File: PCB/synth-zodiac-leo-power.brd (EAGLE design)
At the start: 160 x 100 mm, 29 parts, among them J1 2.5 ID x 5.5 OD, J2 HDR-02P

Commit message: Snapshot of designs so far.
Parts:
- removed J1: 2.5 ID x 5.5 OD, con-jack:KLDX-0202
- added BOOST5: 5V Boost, regulators:POLOLU-U3V40FXX-SMD
- added BOOST9, BOOST9N: BOOST 9V, regulators:POLOLU-U3V40FXX-SMD
- added CONST: Leo, circuit-monkey-zodiac:LEO-CONST
- added GLYPH: Leo, circuit-monkey-zodiac:LEO-GLYPH
- added PCB: PCB FAB, circuit-monkey-zodiac:PENTAGON-40MM-RAD
- added PWR_AMP, PWR_COW, PWR_EG, PWR_KB, PWR_MIDI, PWR_VCA: (no value), con-jst:B4B-PH-SM4
- added VBAT: 2-pin, VT, SMT, con-jst:B2B-PH-SM4
- moved VREG9NEG 88.6 mm to (96.0, 10.0)
- renumbered J2 to 12V
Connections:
- new net VBAT: VBAT.1
- new net VIN: BOOST5.INA, BOOST5.INB, BOOST9.INA, BOOST9.INB, BOOST9N.INA, BOOST9N.INB
- new net VOUT: BOOST5.OUT, BOOST9.OUT, BOOST9N.OUT
- net +5V: now also PWR_AMP.3, PWR_COW.3, PWR_EG.3, PWR_KB.3, PWR_MIDI.3, PWR_VCA.3
- net +9V: now also PWR_AMP.1, PWR_COW.1, PWR_EG.1, PWR_KB.1, PWR_MIDI.1, PWR_VCA.1
- net -9V: now also PWR_AMP.2, PWR_COW.2, PWR_EG.2, PWR_KB.2, PWR_MIDI.2, PWR_VCA.2
- net GND: now also BOOST5.GNDA, BOOST5.GNDB, BOOST9.GNDA, BOOST9.GNDB, BOOST9N.GNDA, BOOST9N.GNDB, PCB.MTG1, PCB.MTG2, PCB.MTG3, PCB.MTG4, PCB.MTG5, PWR_AMP.4, PWR_COW.4, PWR_EG.4, PWR_KB.4, PWR_MIDI.4, PWR_VCA.4, VBAT.2; no longer J1.2A, J1.2B
- net N$1: no longer J1.1A, J1.1B
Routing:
- added copper zone on layer 1, net GND
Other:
- board size 160 x 100 mm -> 76.1 x 72.4 mm

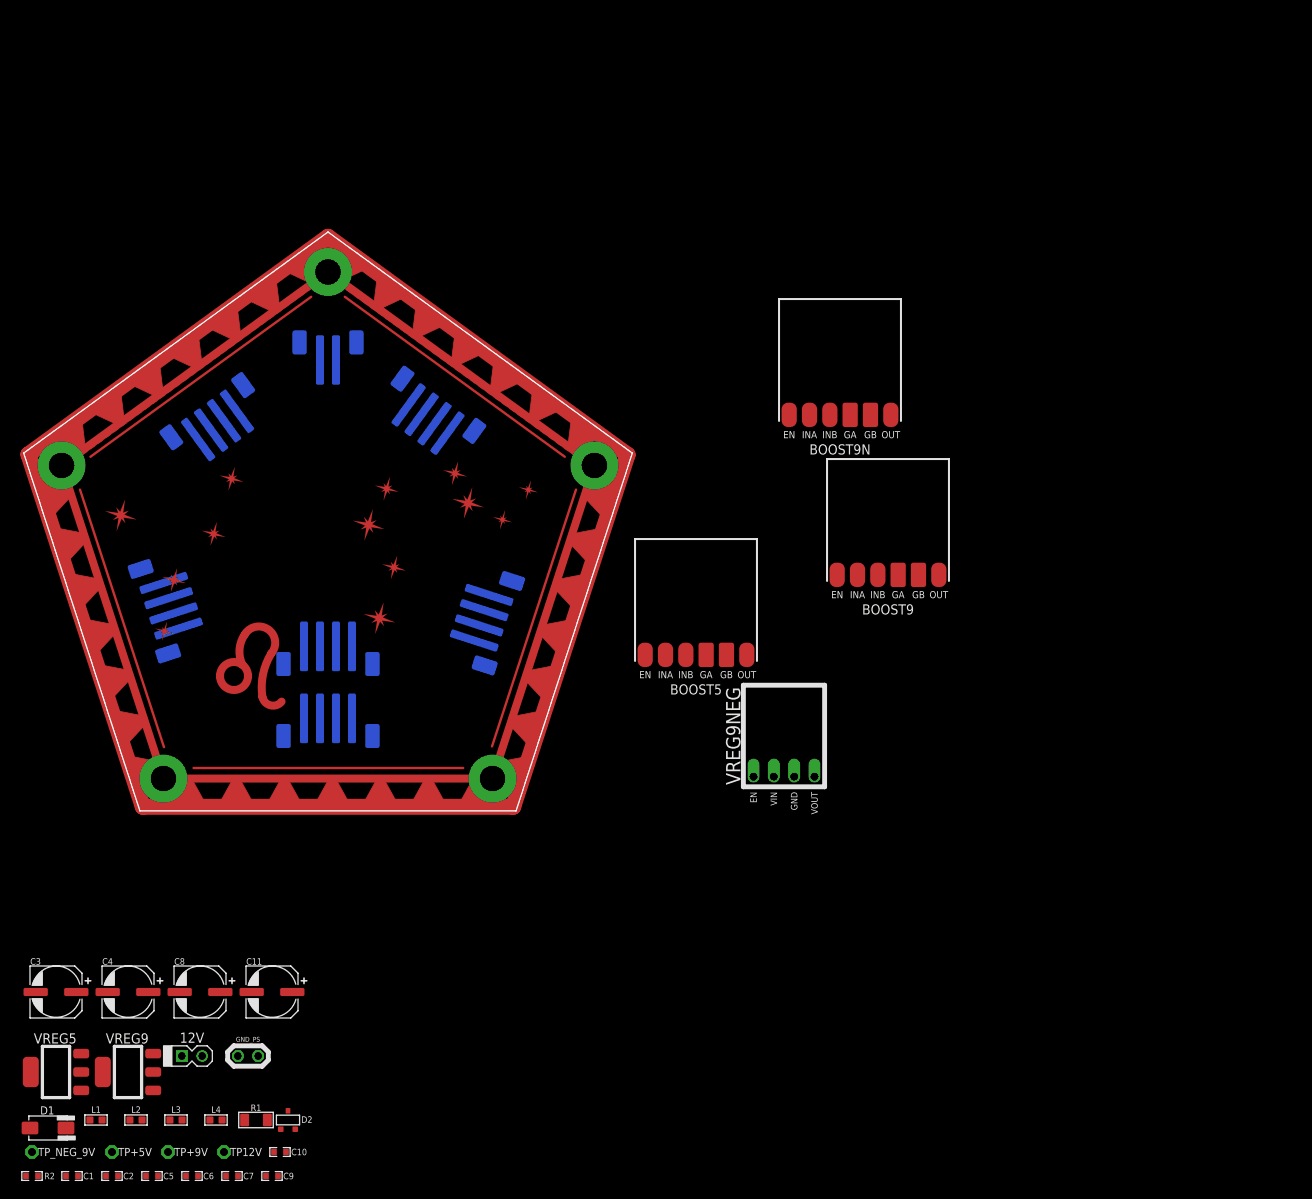
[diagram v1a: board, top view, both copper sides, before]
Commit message: Almost ready for FAB.
Sagittarius was mis-spelled, renamed it.  Taurus is still WIP.
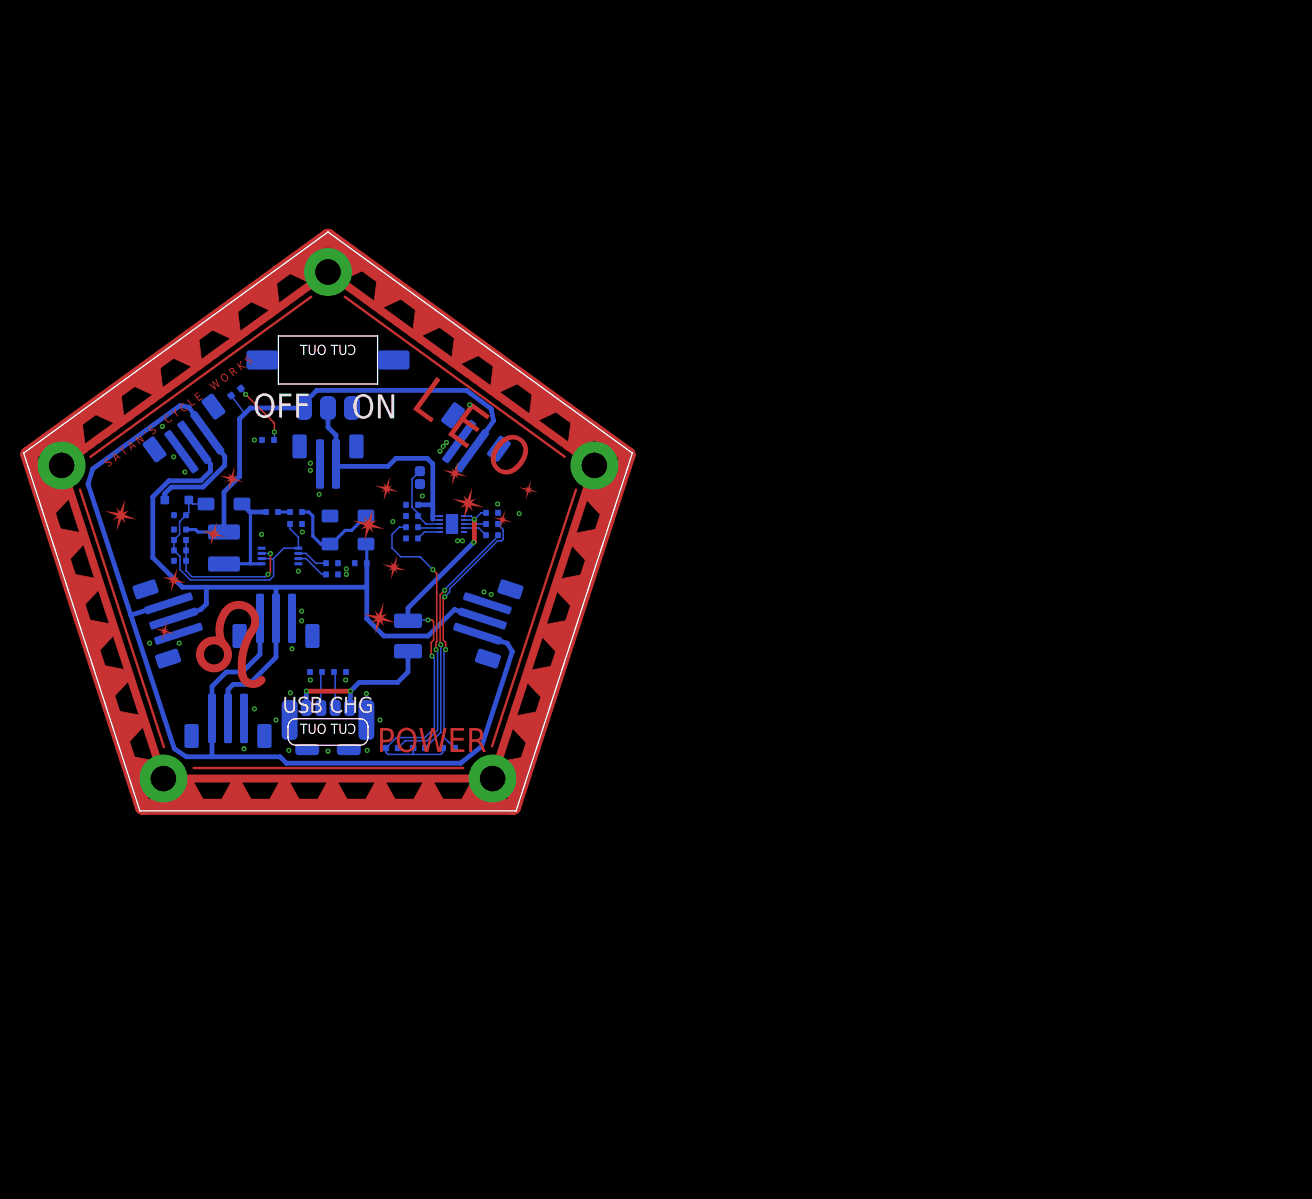
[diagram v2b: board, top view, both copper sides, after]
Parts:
- removed 12V: HDR-02P, con-headers:MA02X1-VT-THD
- removed BOOST5: 5V Boost, regulators:POLOLU-U3V40FXX-SMD
- removed BOOST9, BOOST9N: BOOST 9V, regulators:POLOLU-U3V40FXX-SMD
- removed C10, C9: 0.1uF, rlc:0603-CAP
- removed C11: 22uF/10V, rlc:CAP_ALUM_SMT_6.3
- removed GND_PS: TPTHD-SCOPE-LOOP, con-testpoints:TP-2P-THD
- removed L2, L3, L4: 120OHM-500MA, rlc:L0603
- removed PWR_AMP: (no value), con-jst:B4B-PH-SM4
- removed TP+5V, TP+9V, TP12V, TP_NEG_9V: TPTHD-038, con-testpoints:THD-038MIL-X1
- removed VREG5: 5.0V, regulators:SOT-223
- removed VREG9: 9.0V, regulators:SOT-223
- removed VREG9NEG: -9.0V, regulators:POLOLU-10X13-4P
- added BOOST: MIC2145, regulators:MSOP8-0.65
- added CHRG: RED, led:SMD_0603
- added D3: B140, diodes:SMA
- added D4: 1N4148, diodes:SOD-123
- added DONE: GRN, led:SMD_0603
- added F1: 1.0A, fuse:BOURNS-MF-MSMF
- added GHRG: MCP73833, co-microchip:DFN-10-3X3
- added POK, PON: BLU, led:SMD_0603
- added PWR2AMP: 2-pin, VT, SMT, con-jst:B2B-PH-SM4
- added R10, R9: 5.1K, rlc:0603-RES
- added R11, R6, R7, R8, RPRG: 1K, rlc:0603-RES
- added R3: 120K, rlc:0603-RES
- added R4: 1M, rlc:0603-RES
- added R5: 0.5ohm, rlc:0603-RES
- added RTH: 10K, rlc:0603-RES
- added SW: (no value), switch-thd:SS-12-F45-PNL-SMT
- added THRM, THRM_G: PADSMD-050X050, con-testpoints:SMD-050X050
- added USB: USB-C, PWR, con-usb:UJC-HP-3-SMT-TR-PANEL
- C1: value 0.01uF -> 10uF/6.3V
- C2: value 0.1uF -> 0.01uF
- C3: value 100uF/24V -> 100pF; device rlc:CAP_ALUM_SMT_6.3 -> rlc:0603-CAP
- C4: value 100uF/24V -> 10uF/16V; device rlc:CAP_ALUM_SMT_6.3 -> rlc:0603-CAP
- C5: value 0.1uF -> 10uF
- C6: value 0.1uF -> 2.2uF
- C7: value 0.1uF -> 1uF
- C8: value 22uF/10V -> 1uF; device rlc:CAP_ALUM_SMT_6.3 -> rlc:0603-CAP
- D1: value B130 -> B140
- D2: value 12V -> B140; device diodes:SOT-23 -> diodes:SMA
- L1: value 120OHM-500MA -> 10.0uH; device rlc:L0603 -> rlc:IND-SRN5040
- PWR_COW, PWR_EG, PWR_KB, PWR_MIDI, PWR_VCA: value (none) -> JST, 3P, VT, SMT; device con-jst:B4B-PH-SM4 -> con-jst:B3B-PH-SM4
- R1: value 4.99R -> 100K; device rlc:1206 -> rlc:0603-RES
- R2: value 100K -> 10K
- moved C7 89.0 mm to (59.5, 37.9), flipped to the bottom, turned to 180 degrees
- moved C5 84.9 mm to (35.0, 38.0), flipped to the bottom, turned to 180 degrees
- moved R2 84.0 mm to (39.5, 30.2), flipped to the bottom
- moved C1 81.9 mm to (20.5, 35.8), flipped to the bottom
- moved C2 81.4 mm to (39.5, 31.6), flipped to the bottom, turned to 180 degrees
- moved D1 81.0 mm to (26.0, 39.0), flipped to the bottom
- moved C6 79.5 mm to (43.1, 31.6), flipped to the bottom
- moved R1 74.7 mm to (35.0, 36.5), flipped to the bottom
- moved L1 73.3 mm to (26.0, 33.5), flipped to the bottom, turned to 90 degrees
- moved D2 72.4 mm to (41.5, 34.0), flipped to the bottom
- moved C8 66.4 mm to (49.5, 38.9), flipped to the bottom
- moved C4 60.0 mm to (20.5, 37.6), flipped to the bottom
- moved C3 57.3 mm to (20.5, 33.2), flipped to the bottom, turned to 180 degrees
- moved VBAT 13.0 mm to (39.0, 46.2)
- moved PWR_COW 12.5 mm to (26.5, 10.0)
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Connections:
- removed net +5V: C7.1, C8.+, PWR_AMP.3, PWR_COW.3, PWR_EG.3, PWR_KB.3, PWR_MIDI.3, PWR_VCA.3, TP+5V.1, VREG5.2, VREG5.TAB
- removed net 12V: C5.1, D2.3, L2.1, L3.1, L4.1, R1.2, TP12V.1
- removed net VOUT: BOOST5.OUT, BOOST9.OUT, BOOST9N.OUT
- new net CC1: R9.2, USB.CC1
- new net CC2: R10.2, USB.CC2
- new net FB: BOOST.7, C3.2, R3.2, R4.1
- new net N$10: GHRG.4, R7.2
- new net N$11: GHRG.7, R8.2
- new net N$12: GHRG.8, RTH.2, THRM.1
- new net N$8: GHRG.6, RPRG.2
- new net N$9: GHRG.3, R6.2
- new net RSET: BOOST.3, R2.2
- new net SS: BOOST.2, C2.1
- new net SW: BOOST.5, D1.A, L1.1, R5.1
- new net VOUTA: BOOST.1, BOOST.6, C3.1, C4.1, D1.K, D4.A, R1.2, R4.2
- new net VUSB: C7.1, CHRG.A, DONE.A, F1.2, GHRG.1, GHRG.2, POK.A
- net +9V: now also D4.K; no longer C10.1, C11.+, PWR_AMP.1, TP+9V.1, VREG9.3
- net -9V: now also C6.1, D2.A; no longer PWR_AMP.2, TP_NEG_9V.1, VREG9NEG.GND
- net GND: now also BOOST.4, BOOST.8, C4.2, C8.2, D3.K, GHRG.5, GHRG.PAD, PWR2AMP.2, PWR_COW.3, PWR_EG.3, PWR_KB.3, PWR_MIDI.3, PWR_VCA.3, R1.1, R10.1, R11.1, R2.1, R3.1, R9.1, RPRG.1, RTH.1, THRM_G.1, USB.GND-A, USB.GND-B, USB.PAD1, USB.PAD2; no longer 12V.2, BOOST5.GNDA, BOOST5.GNDB, BOOST9.GNDA, BOOST9.GNDB, BOOST9N.GNDA, BOOST9N.GNDB, C10.2, C11.-, C3.-, C4.-, C5.2, C8.-, C9.2, D2.1, GND_PS.1, GND_PS.2, PWR_AMP.4, PWR_COW.4, PWR_EG.4, PWR_KB.4, PWR_MIDI.4, PWR_VCA.4, VREG5.1, VREG9.2, VREG9.TAB, VREG9NEG.OUT
- net N$1: now also C5.1, R5.2; no longer 12V.1, C1.1, L1.1
- net N$2: now also C5.2, D2.K, D3.A; no longer D1.A, L1.2
- net N$3: now also CHRG.K, R6.1; no longer C2.1, C3.+, C4.+, D1.K, R1.1
- net N$4: now also PON.K, R11.2; no longer C9.1, L3.2, VREG9.1
- net N$5: now also DONE.K, R7.1; no longer C6.1, L2.2, VREG5.3
- net N$6: now also F1.1, USB.VB-A, USB.VB-B; no longer L4.2, R2.1, VREG9NEG.VIN
- net N$7: now also POK.K, R8.1; no longer R2.2, VREG9NEG.SHTDN
- net VBAT: now also C8.1, GHRG.10, GHRG.9, SW.C
- net VIN: now also C1.1, L1.2, PON.A, PWR2AMP.1, SW.B; no longer BOOST5.INA, BOOST5.INB, BOOST9.INA, BOOST9.INB, BOOST9N.INA, BOOST9N.INB
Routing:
- net +9V: track 0.00 -> 153.1 mm
- net -9V: track 0.00 -> 101.7 mm
- net VIN: track 0.00 -> 62.8 mm
- net VUSB: track 0.00 -> 53.9 mm, vias 0 -> 4
- net N$7: track 0.00 -> 36.3 mm, vias 0 -> 2
- net VOUTA: track 0.00 -> 35.4 mm
- net N$3: track 0.00 -> 32.5 mm, vias 0 -> 2
- net VBAT: track 0.00 -> 31.0 mm
- net N$5: track 0.00 -> 30.4 mm, vias 0 -> 2
- net N$6: track 0.00 -> 20.5 mm, vias 0 -> 2
- net FB: track 0.00 -> 18.4 mm, vias 0 -> 2
- net SW: track 0.00 -> 16.5 mm
- net N$2: track 0.00 -> 12.6 mm
- net N$12: track 0.00 -> 9.48 mm
- net N$4: track 0.00 -> 8.16 mm, vias 0 -> 2
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- added copper zone on layer 16, net GND
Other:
- board text added: "L E O"
- board text added: "LEO"
- board text added: "OFF"
- board text added: "ON"
- board text added: "POWER"
- board text added: "Rev. A"
- board text added: "S A T A N ' S C Y C L E W O R K S"
- board text added: "USB CHG"

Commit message: Work in progress for rev A,  VCO rev.B
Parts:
- removed PWR2AMP, VBAT: 2-pin, VT, SMT, con-jst:B2B-PH-SM4
- removed PWR_COW, PWR_EG, PWR_KB, PWR_MIDI, PWR_VCA: JST, 3P, VT, SMT, con-jst:B3B-PH-SM4
- removed SW: (no value), switch-thd:SS-12-F45-PNL-SMT
- added BATT, V2AMP, V2LED: JST, SH, 2P, con-jst:BM02B-SRSS-TB
- added PWR: (no value), switch-thd:SS-12-F45-PNL-SMT
- added PWR01, PWR02, PWR03, PWR04, PWR05, PWR06, PWR07, PWR08, PWR09, PWR10, PWR11: JST SM 3P, con-jst:BM03B-SRSS-TB
- F1: value 1.0A -> 0.5A
- USB: value USB-C, PWR -> USB, POWER; device con-usb:UJC-HP-3-SMT-TR-PANEL -> con-usb:GCT-USB4515-PANEL
- moved D4 27.7 mm to (41.7, 22.2), turned to 90 degrees
- moved C4 20.6 mm to (40.1, 31.4), turned to 180 degrees
- moved R3 17.8 mm to (35.4, 41.6), turned to 0 degrees
- moved C7 16.1 mm to (52.6, 23.3), turned to 270 degrees
- moved R4 16.0 mm to (35.4, 40.4), turned to 180 degrees
- moved C3 15.6 mm to (35.4, 37.9), turned to 0 degrees
- moved R6 15.5 mm to (51.4, 23.3), turned to 90 degrees
- moved CHRG 15.1 mm to (39.0, 7.80)
- moved R7 15.0 mm to (50.2, 23.3), turned to 90 degrees
- moved D3 14.8 mm to (34.9, 24.3), turned to 180 degrees
- moved C6 14.3 mm to (29.2, 28.4)
- moved THRM 13.6 mm to (56.8, 30.8), turned to 90 degrees
- moved C1 13.2 mm to (32.4, 41.6), turned to 180 degrees
- moved THRM_G 13.0 mm to (58.4, 30.8), turned to 90 degrees
- moved PON 12.9 mm to (39.1, 47.4), turned to 180 degrees
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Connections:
- removed net N$6: F1.1, USB.VB-A, USB.VB-B
- new net VBUS: F1.1, USB.VA, USB.VB
- net +9V: now also PWR01.1, PWR02.1, PWR03.1, PWR04.1, PWR05.1, PWR06.1, PWR07.1, PWR08.1, PWR09.1, PWR10.1, PWR11.1; no longer PWR_COW.1, PWR_EG.1, PWR_KB.1, PWR_MIDI.1, PWR_VCA.1
- net -9V: now also PWR01.2, PWR02.2, PWR03.2, PWR04.2, PWR05.2, PWR06.2, PWR07.2, PWR08.2, PWR09.2, PWR10.2, PWR11.2; no longer PWR_COW.2, PWR_EG.2, PWR_KB.2, PWR_MIDI.2, PWR_VCA.2
- net GND: now also BATT.2, PWR01.3, PWR02.3, PWR03.3, PWR04.3, PWR05.3, PWR06.3, PWR07.3, PWR08.3, PWR09.3, PWR10.3, PWR11.3, USB.GNDA, USB.GNDB, USB.P$1, USB.P$2, V2AMP.2, V2LED.2; no longer PWR2AMP.2, PWR_COW.3, PWR_EG.3, PWR_KB.3, PWR_MIDI.3, PWR_VCA.3, USB.GND-A, USB.GND-B, USB.PAD1, USB.PAD2, VBAT.2
- net VBAT: now also BATT.1, PWR.A; no longer SW.C, VBAT.1
- net VIN: now also PWR.C, V2AMP.1, V2LED.1; no longer PWR2AMP.1, SW.B
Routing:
- net -9V: track 101.7 -> 150.0 mm
- net VIN: track 62.8 -> 37.3 mm
- net N$6: track 20.5 -> 0.00 mm, vias 2 -> 0
- net VBUS: track 0.00 -> 19.7 mm
- net VUSB: track 53.9 -> 41.0 mm, vias 4 -> 2
- net N$7: track 36.3 -> 48.1 mm
- net FB: track 18.4 -> 7.12 mm, vias 2 -> 0
- net N$5: track 30.4 -> 21.1 mm
- net +9V: track 153.1 -> 143.9 mm
- net VOUTA: track 35.4 -> 27.3 mm
- net N$3: track 32.5 -> 26.0 mm
- net N$4: track 8.16 -> 1.90 mm, vias 2 -> 0
- net SW: track 16.5 -> 10.6 mm
- net VBAT: track 31.0 -> 33.1 mm
- net SS: track 3.96 -> 1.91 mm
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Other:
- board text added: "3.7V"
- board text removed: "OFF"
- board text removed: "ON"
- board text removed: "USB CHG"

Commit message: Perhaps final Rev. A?
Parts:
- PWR: device switch-thd:SS-12-F45-PNL-SMT -> switch-thd:SS-12-F45-PNL-SMT-2
- USB: value USB, POWER -> USB-C, POWER
- moved PON 1.50 mm to (39.0, 48.9)
- moved R11 1.50 mm to (35.7, 48.9)
- moved USB 0.70 mm to (39.0, 11.7), flipped to the top, turned to 180 degrees
- moved D4 0.30 mm to (41.7, 22.5)
- moved R10 0.20 mm to (37.4, 19.2)
- moved R9 0.20 mm to (40.6, 19.2)
- flipped PWR to the top
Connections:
- net GND: no longer USB.P$1, USB.P$2
- net VBAT: now also PWR.B; no longer PWR.A
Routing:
- net VBAT: track 33.1 -> 34.4 mm
- net VBUS: track 19.7 -> 18.9 mm
- net VIN: track 37.3 -> 36.5 mm
- net CC2: track 4.86 -> 4.34 mm
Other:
- board text added: "HOT GLUE"

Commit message: Tune values and some schematic visual tweaks.
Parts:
- C4: value 10uF/16V -> 10uF/25V
- C5: value 10uF -> 10uF/25V
- C6: value 2.2uF -> 2.2uF/16V
- C7, C8: value 1uF -> 1uF/10V
- R3: value 120K -> 143K
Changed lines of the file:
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@@
 <attribute name="VALUE" x="35.4" y="37.9" size="0.2" layer="28" rot="MR0" align="center"/>
 </element>
-<element name="R3" library="rlc" library_urn="urn:adsk.eagle:library:4192893" package="0603-RES" package3d_urn="urn:adsk.eagle:package:4193040/5" value="120K" x="35.4" y="41.6" smashed="yes" rot="MR0">
+<element name="R3" library="rlc" library_urn="urn:adsk.eagle:library:4192893" package="0603-RES" package3d_urn="urn:adsk.eagle:package:4193040/5" value="143K" x="35.4" y="41.6" smashed="yes" rot="MR0">
 <attribute name="COST01" value="0.10" x="35.4" y="41.6" size="1.778" layer="28" rot="MR0" display="off"/>
 <attribute name="COST10" value="0.05" x="35.4" y="41.6" size="1.778" layer="28" rot="MR0" display="off"/>
@@
 <attribute name="VALUE" x="35.4" y="40.654" size="0.2" layer="28" rot="MR180" align="center"/>
 </element>
-<element name="C4" library="rlc" library_urn="urn:adsk.eagle:library:4192893" package="0603-CAP" package3d_urn="urn:adsk.eagle:package:4193021/5" value="10uF/16V" x="40.1" y="31.4" smashed="yes" rot="MR180">
+<element name="C4" library="rlc" library_urn="urn:adsk.eagle:library:4192893" package="0603-CAP" package3d_urn="urn:adsk.eagle:package:4193021/5" value="10uF/25V" x="40.1" y="31.4" smashed="yes" rot="MR180">
 <attribute name="COST01" value="0.12" x="40.1" y="31.4" size="1.778" layer="28" rot="MR180" display="off"/>
 <attribute name="COST10" value="0.09" x="40.1" y="31.4" size="1.778" layer="28" rot="MR180" display="off"/>
@@
 <attribute name="VALUE" x="34.9" y="24.3" size="0.4064" layer="28" rot="MR180" align="center"/>
 </element>
-<element name="C5" library="rlc" library_urn="urn:adsk.eagle:library:4192893" package="0603-CAP" package3d_urn="urn:adsk.eagle:package:4193021/5" value="10uF" x="29.2" y="30.2" smashed="yes" rot="MR180">
+<element name="C5" library="rlc" library_urn="urn:adsk.eagle:library:4192893" package="0603-CAP" package3d_urn="urn:adsk.eagle:package:4193021/5" value="10uF/25V" x="29.2" y="30.2" smashed="yes" rot="MR180">
 <attribute name="COST01" value="0.12" x="29.2" y="30.2" size="1.778" layer="28" rot="MR180" display="off"/>
 <attribute name="COST10" value="0.09" x="29.2" y="30.2" size="1.778" layer="28" rot="MR180" display="off"/>
@@
 <attribute name="VALUE" x="29.2" y="30.2" size="0.2" layer="28" rot="MR180" align="center"/>
 </element>
-<element name="C6" library="rlc" library_urn="urn:adsk.eagle:library:4192893" package="0603-CAP" package3d_urn="urn:adsk.eagle:package:4193021/5" value="2.2uF" x="29.2" y="28.4" smashed="yes" rot="MR0">
+<element name="C6" library="rlc" library_urn="urn:adsk.eagle:library:4192893" package="0603-CAP" package3d_urn="urn:adsk.eagle:package:4193021/5" value="2.2uF/16V" x="29.2" y="28.4" smashed="yes" rot="MR0">
 <attribute name="COST01" value="0.12" x="29.2" y="28.4" size="1.778" layer="28" rot="MR0" display="off"/>
 <attribute name="COST10" value="0.09" x="29.2" y="28.4" size="1.778" layer="28" rot="MR0" display="off"/>
@@
 <attribute name="VALUE" x="40.4" y="22.45" size="0.3048" layer="28" font="vector" rot="MR90" align="center"/>
 </element>
-<element name="C7" library="rlc" library_urn="urn:adsk.eagle:library:4192893" package="0603-CAP" package3d_urn="urn:adsk.eagle:package:4193021/5" value="1uF" x="52.6" y="23.3" smashed="yes" rot="MR270">
+<element name="C7" library="rlc" library_urn="urn:adsk.eagle:library:4192893" package="0603-CAP" package3d_urn="urn:adsk.eagle:package:4193021/5" value="1uF/10V" x="52.6" y="23.3" smashed="yes" rot="MR270">
 <attribute name="COST01" value="0.12" x="52.6" y="23.3" size="1.778" layer="28" rot="MR270" display="off"/>
 <attribute name="COST10" value="0.09" x="52.6" y="23.3" size="1.778" layer="28" rot="MR270" display="off"/>
@@
 <attribute name="VALUE" x="51.4" y="31.6" size="0.2" layer="28" rot="MR270" align="center"/>
 </element>
-<element name="C8" library="rlc" library_urn="urn:adsk.eagle:library:4192893" package="0603-CAP" package3d_urn="urn:adsk.eagle:package:4193021/5" value="1uF" x="54.2" y="31.6" smashed="yes" rot="MR90">
+<element name="C8" library="rlc" library_urn="urn:adsk.eagle:library:4192893" package="0603-CAP" package3d_urn="urn:adsk.eagle:package:4193021/5" value="1uF/10V" x="54.2" y="31.6" smashed="yes" rot="MR90">
 <attribute name="COST01" value="0.12" x="54.2" y="31.6" size="1.778" layer="28" rot="MR90" display="off"/>
 <attribute name="COST10" value="0.09" x="54.2" y="31.6" size="1.778" layer="28" rot="MR90" display="off"/>

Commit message: Update component value for charging rate.
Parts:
- RPRG: value 1K -> 4K
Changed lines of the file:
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@@
 <attribute name="VALUE" x="54.2" y="31.6" size="0.2" layer="28" rot="MR90" align="center"/>
 </element>
-<element name="RPRG" library="rlc" library_urn="urn:adsk.eagle:library:4192893" package="0603-RES" package3d_urn="urn:adsk.eagle:package:4193040/5" value="1K" x="50.2" y="31.6" smashed="yes" rot="MR270">
+<element name="RPRG" library="rlc" library_urn="urn:adsk.eagle:library:4192893" package="0603-RES" package3d_urn="urn:adsk.eagle:package:4193040/5" value="4K" x="50.2" y="31.6" smashed="yes" rot="MR270">
 <attribute name="COST01" value="0.10" x="50.2" y="31.6" size="1.778" layer="28" rot="MR270" display="off"/>
 <attribute name="COST10" value="0.05" x="50.2" y="31.6" size="1.778" layer="28" rot="MR270" display="off"/>
